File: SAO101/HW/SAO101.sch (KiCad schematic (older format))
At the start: 43 parts, among them J1 USB_B_Micro, J2 SAO_Conn, U1 AMS1117-3.3, U2 MCP23017_SS

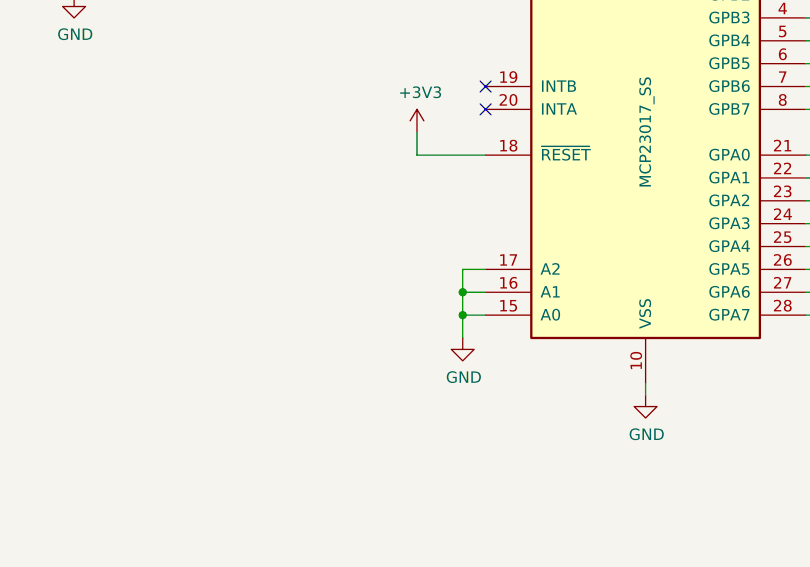
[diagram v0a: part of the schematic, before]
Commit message: update schematic with I2C address
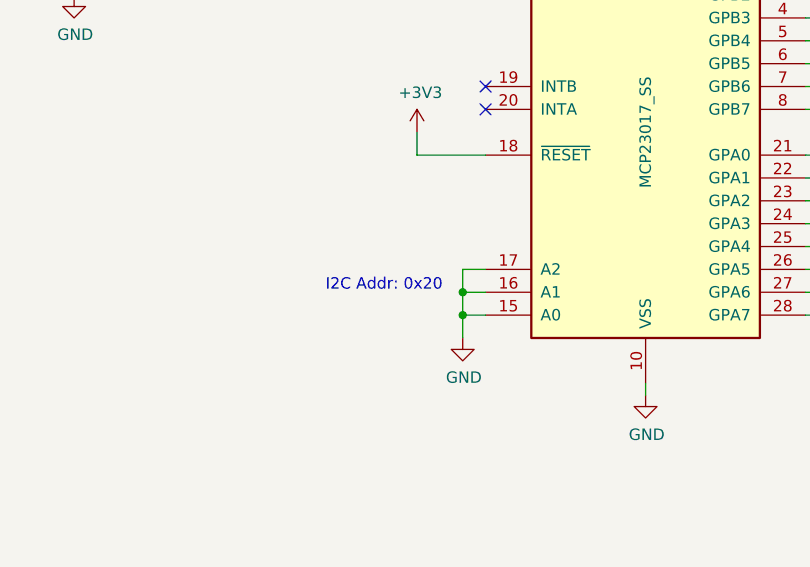
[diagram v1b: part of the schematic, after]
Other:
- note added: "I2C Addr: 0x20"
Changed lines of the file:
@@
 	1    0    0    -1
 $EndComp
+Text Notes 4150 4000 0    50   ~ 0
+I2C Addr: 0x20
 $EndSCHEMATC
